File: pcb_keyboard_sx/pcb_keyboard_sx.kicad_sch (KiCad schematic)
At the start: 123 parts, among them SW1 BOOT button, U1 Pico, U2 TRRS

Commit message: level shifter added also for sx part
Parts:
- added JP4: Jumper_2_Bridged, Jumper:SolderJumper-2_P1.3mm_Bridged2Bar_Pad1.0x1.5mm, symbol Jumper:Jumper_2_Bridged
- added U3: 74LVC1G34, Package_TO_SOT_SMD:SOT-353_SC-70-5_Handsoldering, symbol 74xGxx:74LVC1G34
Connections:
- net +5V: now also U3.5 (VCC)
- net GND: now also U3.3 (GND)
- net LED_GPIO renamed LED 3.3V
- net LED 3.3V: now also JP4.2 (B), U3.2; no longer JP3.1 (A)
- new net LED 5V: JP3.1 (A), JP4.1 (A), U3.4

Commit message: added d+ and d- bus
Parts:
- added TP6, TP7, TP8, TP9: TestPoint, Connector_PinHeader_2.54mm:PinHeader_1x01_P2.54mm_Vertical, symbol Connector:TestPoint
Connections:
- new net Data+: TP6.1, TP7.1
- new net Data-: TP8.1, TP9.1

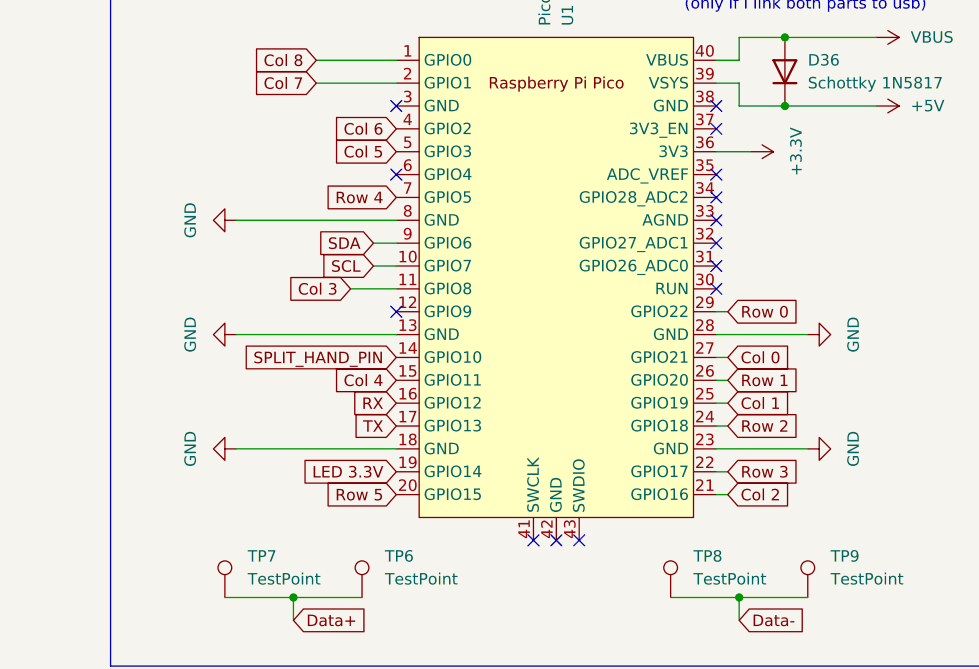
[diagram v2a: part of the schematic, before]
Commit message: stessi GPIO per dx e sx
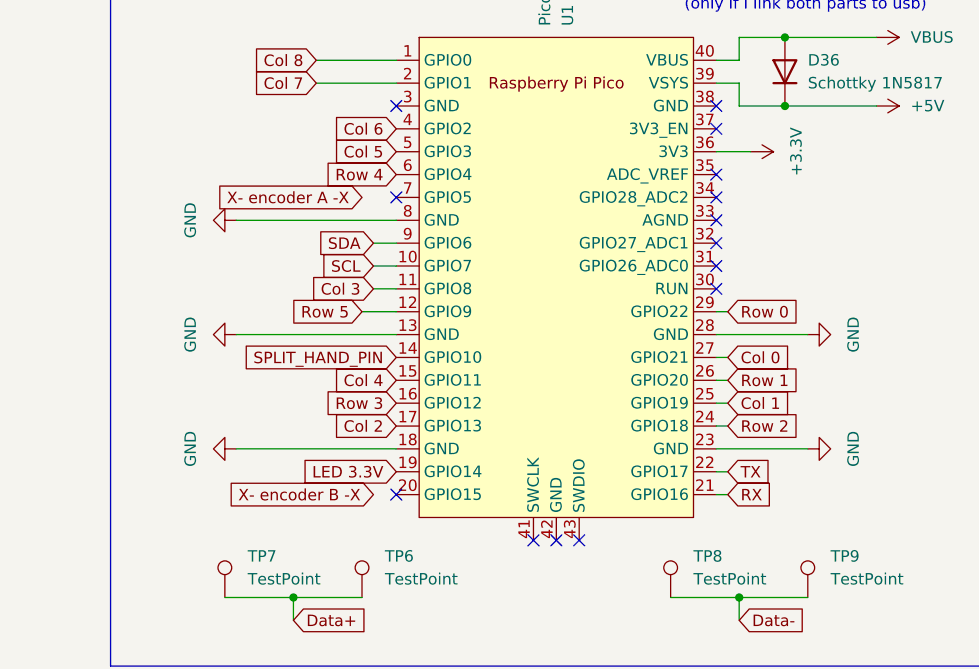
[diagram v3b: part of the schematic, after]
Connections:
- net Col 2: now also U1.17 (GPIO13); no longer U1.21 (GPIO16)
- net RX: now also U1.21 (GPIO16); no longer U1.16 (GPIO12)
- net Row 3: now also U1.16 (GPIO12); no longer U1.22 (GPIO17)
- net Row 4: now also U1.6 (GPIO4); no longer U1.7 (GPIO5)
- net Row 5: now also U1.12 (GPIO9); no longer U1.20 (GPIO15)
- net TX: now also U1.22 (GPIO17); no longer U1.17 (GPIO13)
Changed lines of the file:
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@@
 	)
 	(no_connect
-		(at 318.77 260.35)
+		(at 318.77 280.67)
 	)
 	(no_connect
@@
 	)
 	(no_connect
-		(at 318.77 245.11)
+		(at 318.77 247.65)
 	)
 	(no_connect
@@
 	(wire
 		(pts
+			(xy 314.96 260.35) (xy 318.77 260.35)
+		)
+		(stroke
+			(width 0)
+			(type default)
+		)
+	)
+	(wire
+		(pts
 			(xy 134.62 53.34) (xy 160.02 53.34)
 		)
@@
 	(wire
 		(pts
-			(xy 313.69 257.81) (xy 318.77 257.81)
+			(xy 316.23 257.81) (xy 318.77 257.81)
 		)
 		(stroke
@@
 		)
 	)
-	(global_label "LED 5V"
+	(global_label "Row 4"
 		(shape input)
-		(at 113.03 373.38 270)
+		(at 318.77 245.11 180)
 		(fields_autoplaced yes)
 		(effects
@@
 		)
 		(property "Intersheetrefs" "${INTERSHEET_REFS}"
-			(at 113.03 383.078 90)
+			(at 309.8582 245.11 0)
 			(effects
 				(font
@@
 		)
 	)
-	(global_label "SCL"
+	(global_label "LED 5V"
 		(shape input)
-		(at 316.23 255.27 180)
+		(at 113.03 373.38 270)
 		(fields_autoplaced yes)
 		(effects
@@
 		)
 		(property "Intersheetrefs" "${INTERSHEET_REFS}"
-			(at 309.7372 255.27 0)
+			(at 113.03 383.078 90)
 			(effects
 				(font
@@
 		)
 	)
-	(global_label "Row 0"
+	(global_label "SCL"
 		(shape input)
-		(at 355.6 260.35 0)
+		(at 316.23 255.27 180)
 		(fields_autoplaced yes)
 		(effects
@@
 				(size 1.27 1.27)
 			)
-			(justify left)
+			(justify right)
 		)
 		(property "Intersheetrefs" "${INTERSHEET_REFS}"
-			(at 364.5118 260.35 0)
+			(at 309.7372 255.27 0)
 			(effects
 				(font
 					(size 1.27 1.27)
 				)
-				(justify left)
+				(justify right)
 				(hide yes)
 			)
 		)
 	)
-	(global_label "Row 3"
+	(global_label "Row 0"
 		(shape input)
-		(at 355.6 278.13 0)
+		(at 355.6 260.35 0)
 		(fields_autoplaced yes)
 		(effects
@@
 		)
 		(property "Intersheetrefs" "${INTERSHEET_REFS}"
-			(at 364.5118 278.13 0)
+			(at 364.5118 260.35 0)
 			(effects
 				(font
@@
 		)
 	)
+	(global_label "RX"
+		(shape input)
+		(at 355.6 280.67 0)
+		(fields_autoplaced yes)
+		(effects
+			(font
+				(size 1.27 1.27)
+			)
+			(justify left)
+		)
+		(property "Intersheetrefs" "${INTERSHEET_REFS}"
+			(at 361.0647 280.67 0)
+			(effects
+				(font
+					(size 1.27 1.27)
+				)
+				(justify left)
+				(hide yes)
+			)
+		)
+	)
 	(global_label "Col 4"
 		(shape input)
@@
 		)
 	)
-	(global_label "Row 5"
-		(shape input)
-		(at 318.77 280.67 180)
-		(fields_autoplaced yes)
-		(effects
-			(font
-				(size 1.27 1.27)
-			)
-			(justify right)
-		)
-		(property "Intersheetrefs" "${INTERSHEET_REFS}"
-			(at 309.8582 280.67 0)
-			(effects
-				(font
-					(size 1.27 1.27)
-				)
-				(justify right)
-				(hide yes)
-			)
-		)
-	)
 	(global_label "LED 3.3V"
 		(shape input)
@@
 	(global_label "Col 3"
 		(shape input)
-		(at 313.69 257.81 180)
+		(at 316.23 257.81 180)
 		(fields_autoplaced yes)
 		(effects
@@
 		)
 		(property "Intersheetrefs" "${INTERSHEET_REFS}"
-			(at 305.4435 257.81 0)
+			(at 307.9835 257.81 0)
 			(effects
 				(font
@@
 		)
 	)
-	(global_label "RX"
+	(global_label "Row 1"
 		(shape input)
-		(at 318.77 270.51 180)
+		(at 355.6 267.97 0)
 		(fields_autoplaced yes)
 		(effects
@@
 				(size 1.27 1.27)
 			)
-			(justify right)
+			(justify left)
 		)
 		(property "Intersheetrefs" "${INTERSHEET_REFS}"
-			(at 313.3053 270.51 0)
+			(at 364.5118 267.97 0)
 			(effects
 				(font
 					(size 1.27 1.27)
 				)
-				(justify right)
+				(justify left)
 				(hide yes)
 			)
 		)
 	)
-	(global_label "Row 1"
+	(global_label "X- encoder A -X"
 		(shape input)
-		(at 355.6 267.97 0)
+		(at 314.96 247.65 180)
 		(fields_autoplaced yes)
 		(effects
@@
 				(size 1.27 1.27)
 			)
-			(justify left)
+			(justify right)
 		)
 		(property "Intersheetrefs" "${INTERSHEET_REFS}"
-			(at 364.5118 267.97 0)
+			(at 294.9206 247.65 0)
 			(effects
 				(font
 					(size 1.27 1.27)
 				)
-				(justify left)
+				(justify right)
 				(hide yes)
 			)
@@
 		)
 	)
-	(global_label "Row 4"
+	(global_label "Col 2"
 		(shape input)
-		(at 318.77 247.65 180)
+		(at 318.77 273.05 180)
 		(fields_autoplaced yes)
 		(effects
@@
 		)
 		(property "Intersheetrefs" "${INTERSHEET_REFS}"
-			(at 309.8582 247.65 0)
+			(at 310.5235 273.05 0)
 			(effects
 				(font
@@
 		)
 	)
-	(global_label "TX"
+	(global_label "Row 3"
 		(shape input)
-		(at 318.77 273.05 180)
+		(at 318.77 270.51 180)
 		(fields_autoplaced yes)
 		(effects
@@
 		)
 		(property "Intersheetrefs" "${INTERSHEET_REFS}"
-			(at 313.6077 273.05 0)
+			(at 309.8582 270.51 0)
 			(effects
 				(font
@@
 		)
 	)
-	(global_label "Col 2"
+	(global_label "Row 5"
 		(shape input)
-		(at 355.6 280.67 0)
+		(at 314.96 260.35 180)
 		(fields_autoplaced yes)
 		(effects
@@
 				(size 1.27 1.27)
 			)
-			(justify left)
+			(justify right)
 		)
 		(property "Intersheetrefs" "${INTERSHEET_REFS}"
-			(at 363.8465 280.67 0)
+			(at 306.0482 260.35 0)
 			(effects
 				(font
 					(size 1.27 1.27)
 				)
-				(justify left)
+				(justify right)
 				(hide yes)
 			)
@@
 		)
 	)
+	(global_label "X- encoder B -X"
+		(shape input)
+		(at 316.23 280.67 180)
+		(fields_autoplaced yes)
+		(effects
+			(font
+				(size 1.27 1.27)
+			)
+			(justify right)
+		)
+		(property "Intersheetrefs" "${INTERSHEET_REFS}"
+			(at 296.0092 280.67 0)
+			(effects
+				(font
+					(size 1.27 1.27)
+				)
+				(justify right)
+				(hide yes)
+			)
+		)
+	)
 	(global_label "Data-"
 		(shape input)
@@
 				(hide yes)
 			)
+		)
+	)
+	(global_label "TX"
+		(shape input)
+		(at 355.6 278.13 0)
+		(fields_autoplaced yes)
+		(effects
+			(font
+				(size 1.27 1.27)
+			)
+			(justify left)
+		)
+		(property "Intersheetrefs" "${INTERSHEET_REFS}"
+			(at 360.7623 278.13 0)
+			(effects
+				(font
+					(size 1.27 1.27)
+				)
+				(justify left)
+				(hide yes)
+			)
